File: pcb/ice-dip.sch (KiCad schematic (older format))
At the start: 40 parts, among them J1 Pin1-20, J2 Pin21-40, U1 ICE40UP5K-SG48ITR50, U2 W25Q16JVSNIQ, U3 LDL1117S33R, U4 MCP1700T-1202E/TT, U5 SN74CBTD3861PWR, U6 SN74CBTD3861PWR, U7 SN74CBTD3861PWR, U8 SN74CBTD3861PWR, X1 SG-5032CAN

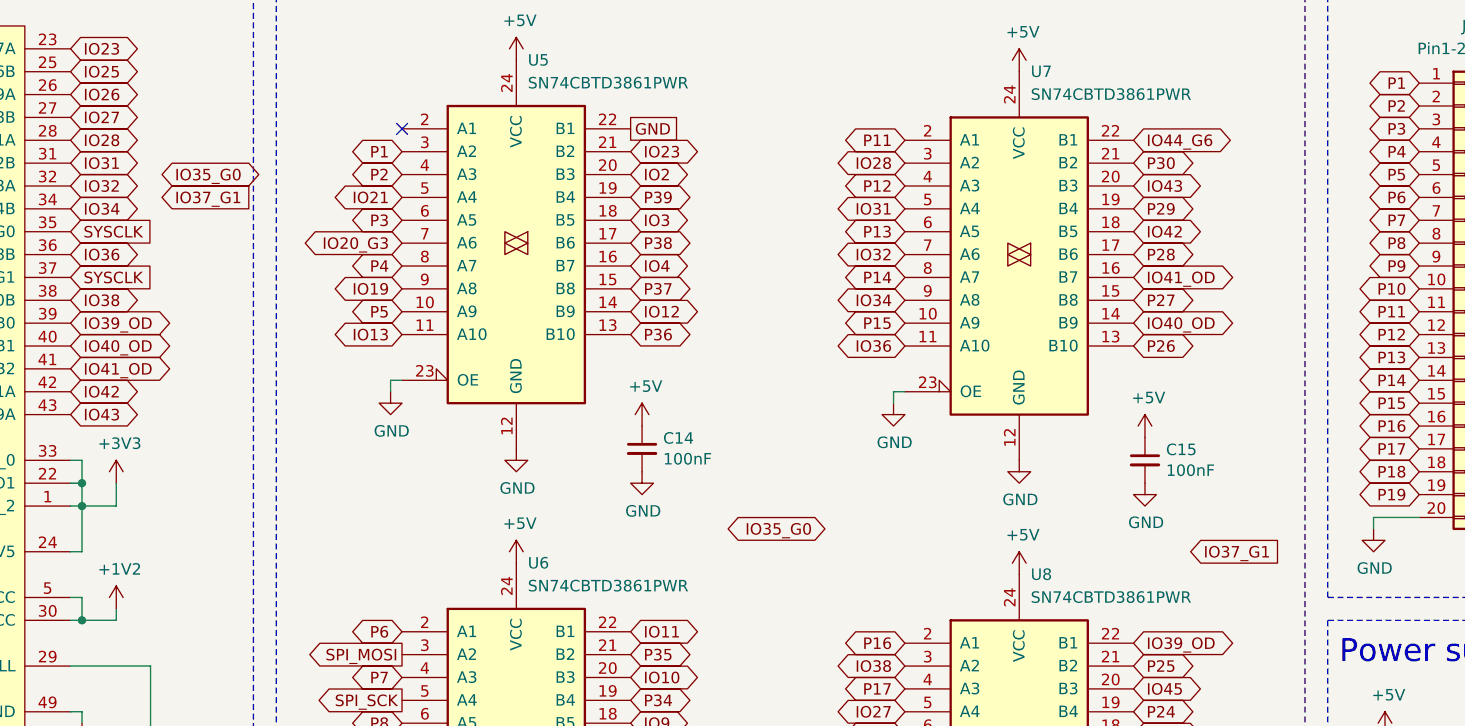
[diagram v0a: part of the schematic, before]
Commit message: Library for ICE-DIP component. Fixing some small issues.
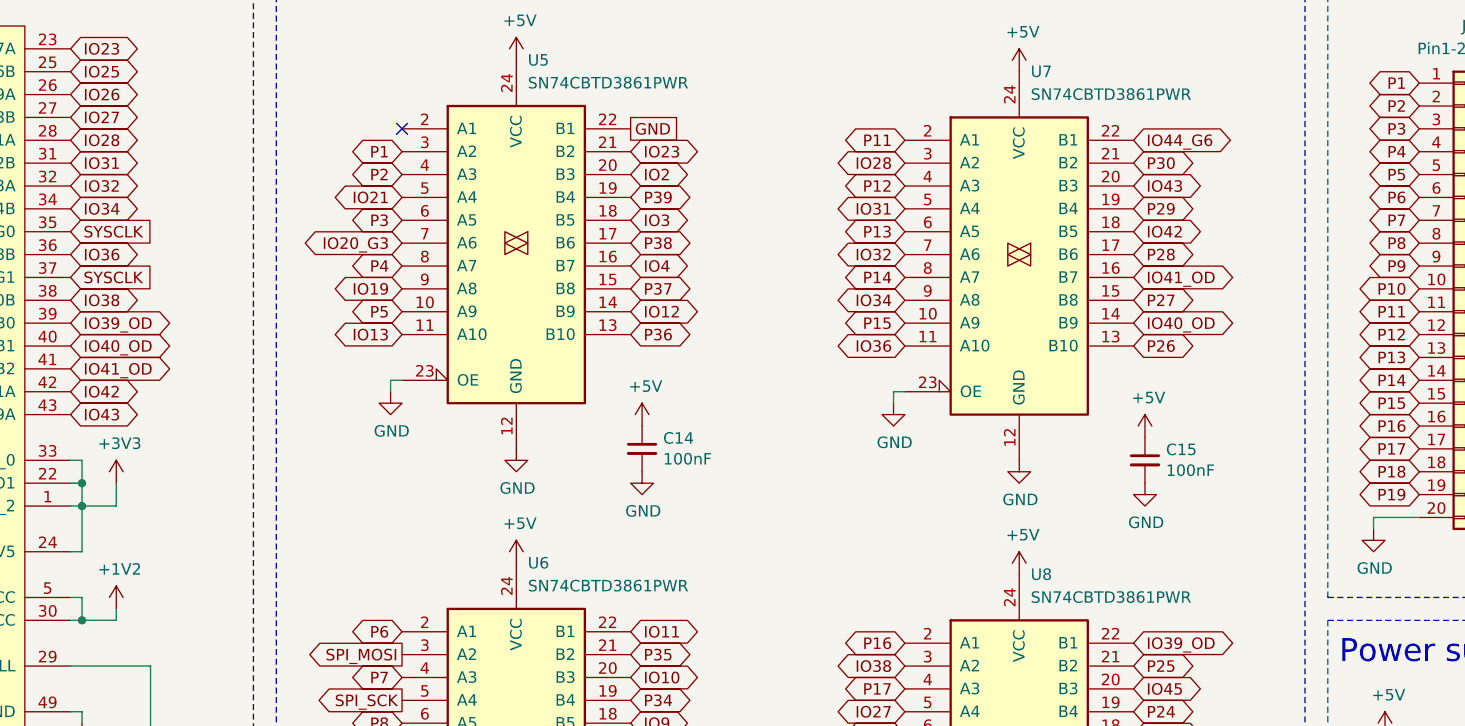
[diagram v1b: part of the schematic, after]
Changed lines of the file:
@@
 Text GLabel 3000 1200 2    50   BiDi ~ 0
 IO26
-Text GLabel 3400 1550 2    50   BiDi ~ 0
-IO35_G0
 Wire Wire Line
 	3000 3700 3350 3700
@@
 Wire Wire Line
 	1200 5800 1150 5800
-Text GLabel 3400 1650 2    50   Input ~ 0
-IO37_G1
 Text GLabel 3000 1300 2    50   BiDi ~ 0
 IO27
@@
 Text GLabel 5450 1350 2    50   UnSpc ~ 0
 GND
-Text GLabel 7900 3200 2    50   Input ~ 0
-IO37_G1
 Text GLabel 6650 2300 0    50   BiDi ~ 0
 IO36
 Text GLabel 6650 3700 0    50   BiDi ~ 0
 IO38
-Text GLabel 6300 3100 0    50   BiDi ~ 0
-IO35_G0
 Text GLabel 6650 2100 0    50   BiDi ~ 0
 IO34
